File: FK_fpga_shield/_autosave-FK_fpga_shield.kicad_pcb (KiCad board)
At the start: 4 copper layers, 182 x 125 mm, 174 parts, among them J0 USB_B_Mini, J1 molex-51382-0400-microclasp, J10 molex-51382-0400-microclasp, J11 molex-51382-0400-microclasp, J12 molex-51382-0400-microclasp, J13 molex-51382-0400-microclasp, J14 molex-51382-0400-microclasp, J15 molex-51382-0400-microclasp, J16 molex-51382-0400-microclasp, J17 molex-51382-0400-microclasp, J18 molex-51382-0400-microclasp, J19 molex-51382-0400-microclasp, J2 molex-51382-0400-microclasp, J20 molex-51382-0400-microclasp, J21 molex-51382-0400-microclasp, J22 molex-51382-0400-microclasp, J23 molex-51382-0400-microclasp, J24 molex-51382-0400-microclasp, J25 molex-51382-0400-microclasp, J26 molex-51382-0400-microclasp, J27 molex-51382-0400-microclasp, J28 molex-51382-0400-microclasp, J29 molex-51382-0400-microclasp, J3 molex-51382-0400-microclasp, J30 molex-51382-0400-microclasp, J31 molex-51382-0400-microclasp, J32 molex-51382-0400-microclasp, J33 molex-51382-0400-microclasp, J34 molex-51382-0400-microclasp, J35 molex-51382-0400-microclasp, J36 Barrel_Jack_MountingPin, J37 Conn_02x04_Top_Bottom, J4 molex-51382-0400-microclasp, J5 molex-51382-0400-microclasp, J6 molex-51382-0400-microclasp, J7 molex-51382-0400-microclasp, J8 molex-51382-0400-microclasp, J9 molex-51382-0400-microclasp, U1 FT232RL, U2 nvt2010pw, U3 nvt2010pw, U4 nvt2010pw, U5 nvt2010pw, U6 nvt2010pw, U7 nvt2010pw, U8 nvt2010pw, Y1 DNP_(12MHz)

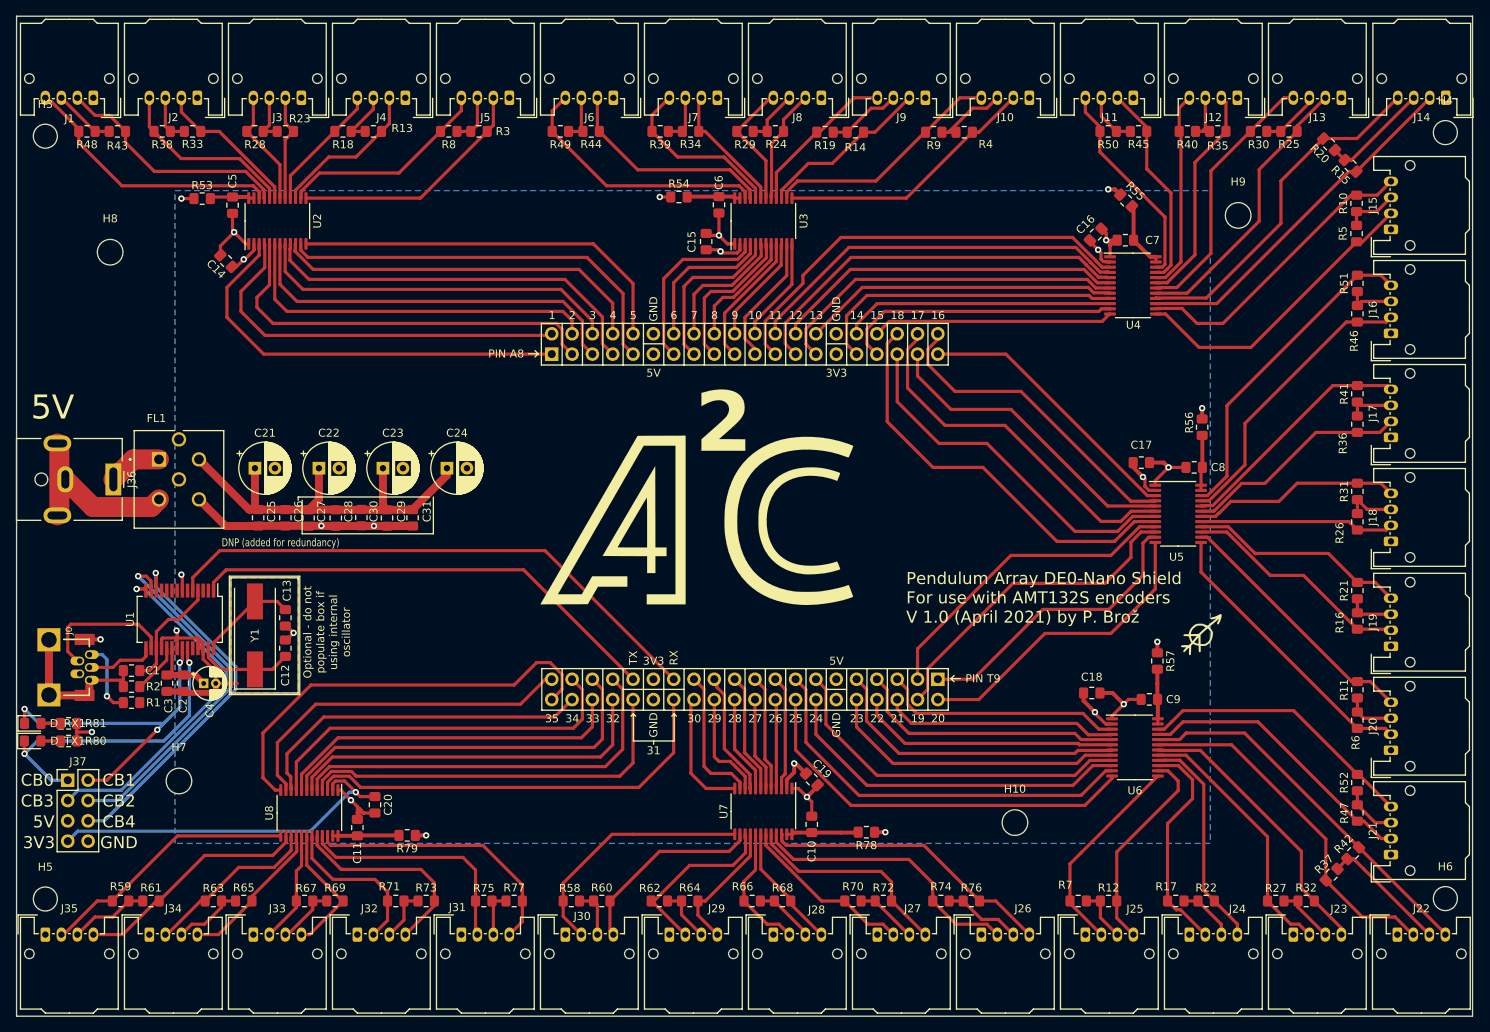
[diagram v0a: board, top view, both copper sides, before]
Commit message: mounting holes, silkscreen
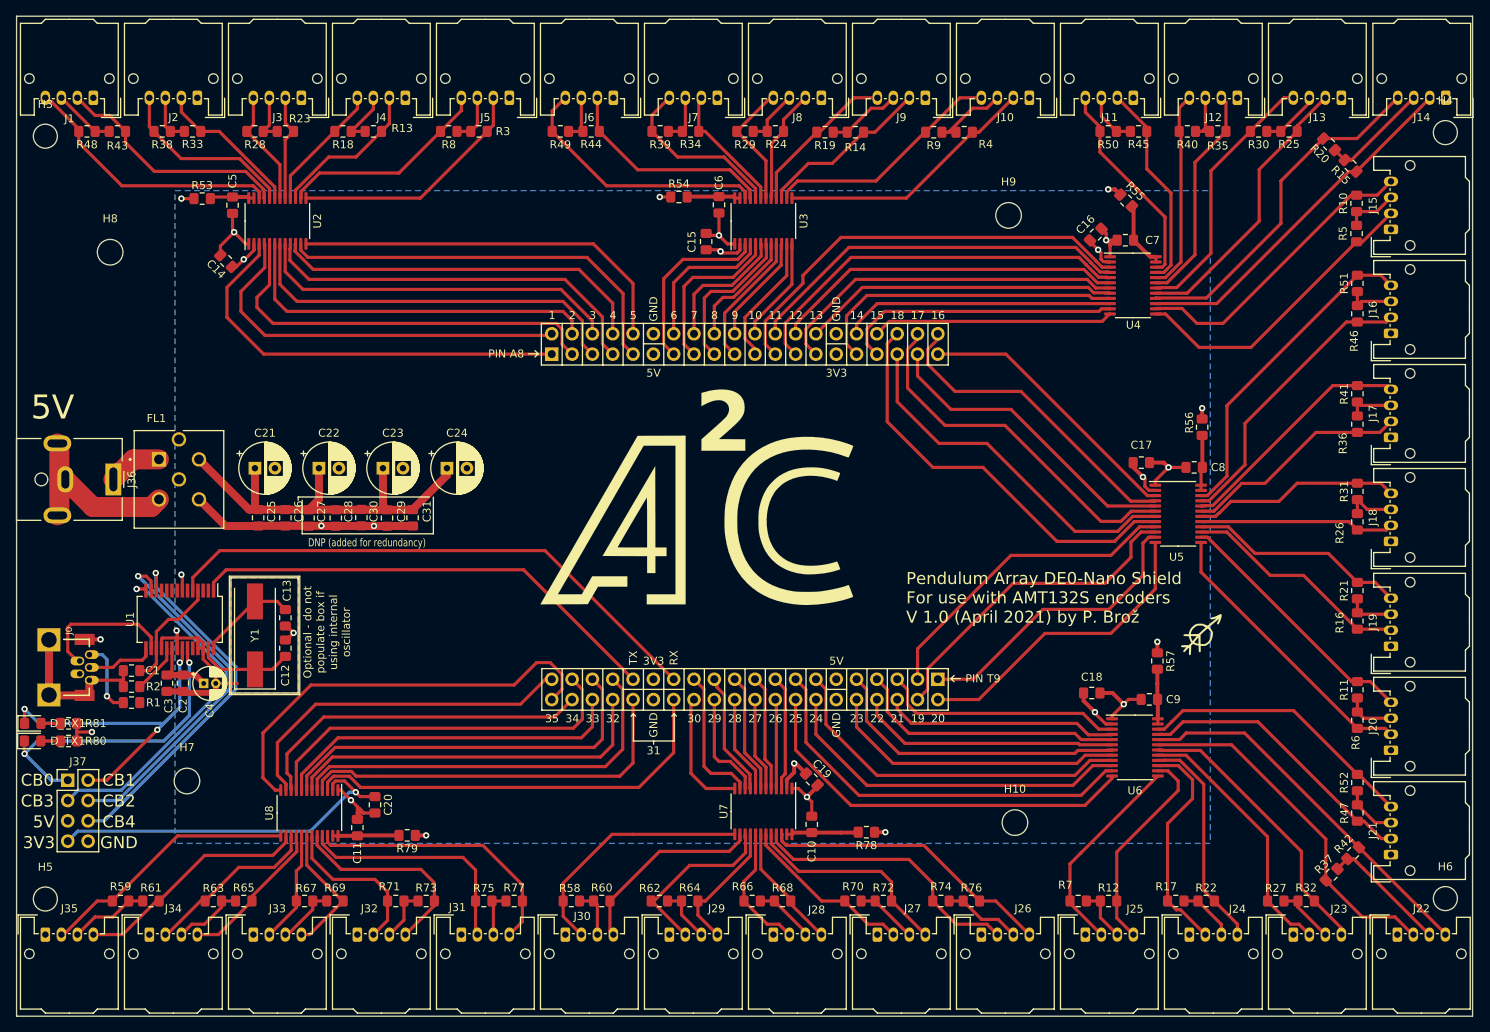
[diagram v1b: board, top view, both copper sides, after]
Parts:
- moved H9 28.7 mm to (199.2, 63.5)
- moved H7 1.00 mm to (96.5, 134.2)
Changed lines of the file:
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@@
   )
   (module MountingHole:MountingHole_3.2mm_M3 (layer F.Cu)
-    (at 227.9 63.5)
+    (at 199.2 63.5)
     (descr "Mounting Hole 3.2mm, no annular, M3")
     (tags "mounting hole 3.2mm no annular m3")
@@
   )
   (module MountingHole:MountingHole_3.2mm_M3 (layer F.Cu)
-    (at 95.5 134.2)
+    (at 96.5 134.2)
     (descr "Mounting Hole 3.2mm, no annular, M3")
     (tags "mounting hole 3.2mm no annular m3")
@@
   (gr_line (start 140.8 82.2) (end 143.4 82.2) (layer F.SilkS) (width 0.12))
   (gr_line (start 140.8 77) (end 140.8 82.2) (layer F.SilkS) (width 0.12))
-  (gr_text "DNP (added for redundancy)" (at 108.2 104.4) (layer F.SilkS)
+  (gr_text "DNP (added for redundancy)" (at 119 104.4) (layer F.SilkS)
     (effects (font (size 1 0.75) (thickness 0.15)))
   )
